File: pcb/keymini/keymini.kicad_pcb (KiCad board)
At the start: 2 copper layers, 205.4 x 88.6 mm, 86 parts, among them J1 USB_C_Receptacle_USB2.0_16P, SW1A1 SW_Push, SW1B1 SW_Push, SW1C1 SW_Push, SW1D1 SW_Push, SW1E1 SW_Push, SW1F1 SW_Push, SW1G1 SW_Push, SW1H1 SW_Push, SW1I1 SW_Push, SW1J1 SW_Push, SW2A1 SW_Push, SW2B1 SW_Push, SW2C1 SW_Push, SW2D1 SW_Push, SW2E1 SW_Push, SW2F1 SW_Push, SW2G1 SW_Push, SW2H1 SW_Push, SW2I1 SW_Push, SW2J1 SW_Push, SW3A1 SW_Push, SW3B1 SW_Push, SW3C1 SW_Push, SW3D1 SW_Push, SW3E1 SW_Push, SW3F1 SW_Push, SW3G1 SW_Push, SW3H1 SW_Push, SW3I1 SW_Push, SW3J1 SW_Push, SW4C1 SW_Push, SW4D1 SW_Push, SW4E1 SW_Push, SW4F1 SW_Push, SW4G1 SW_Push, SW4H1 SW_Push, U1 STM32F072CBT6, U2 XC6206P332MR

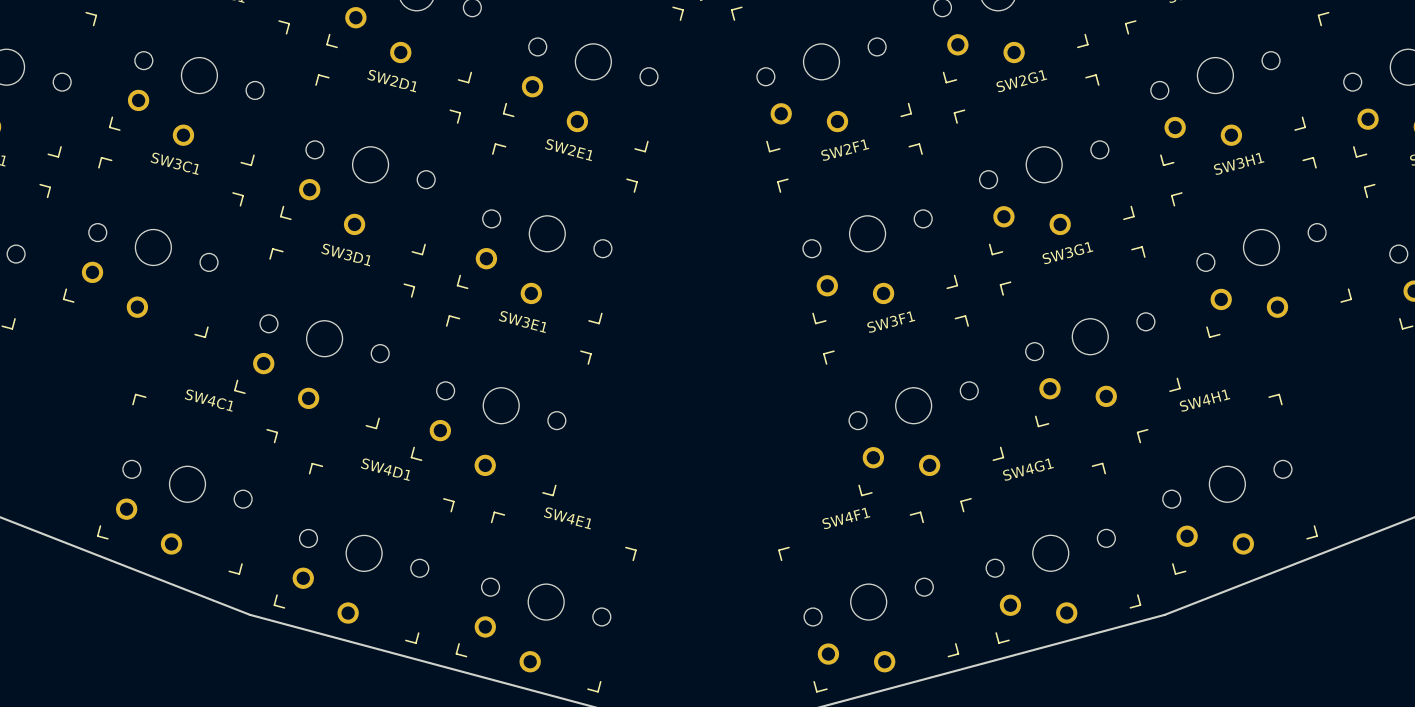
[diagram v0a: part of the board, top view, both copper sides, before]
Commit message: key placement corrections
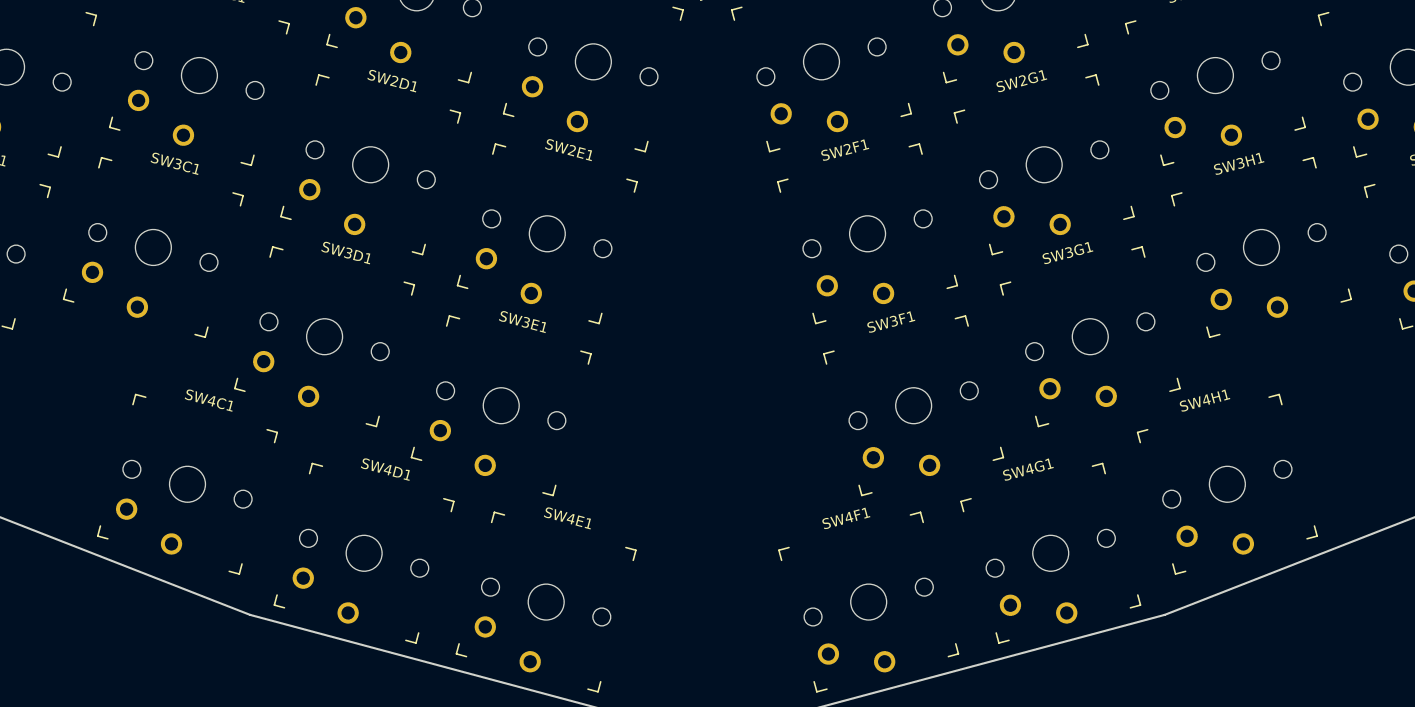
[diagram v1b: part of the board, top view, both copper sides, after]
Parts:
- moved SW3D1 0.19 mm to (113.4, 72.1)
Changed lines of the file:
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@@
 	(footprint "switch:SW_PG1350"
 		(layer "F.Cu")
-		(at 97.087 63.61 -15)
+		(at 97.086 63.609 -15)
 		(descr "Kailh \"Choc\" PG1350 keyswitch")
 		(tags "kailh,choc")
@@
 	(footprint "switch:SW_PG1350"
 		(layer "F.Cu")
-		(at 117.214 92.824 -15)
+		(at 117.214 92.814 -15)
 		(descr "Kailh \"Choc\" PG1350 keyswitch")
 		(tags "kailh,choc")
@@
 	(footprint "switch:SW_PG1350"
 		(layer "F.Cu")
-		(at 113.438 72.32 -15)
+		(at 113.438 72.132 -15)
 		(descr "Kailh \"Choc\" PG1350 keyswitch")
 		(tags "kailh,choc")
@@
 	(footprint "switch:SW_PG1350"
 		(layer "F.Cu")
-		(at 117.828 55.711 -15)
+		(at 117.838 55.711 -15)
 		(descr "Kailh \"Choc\" PG1350 keyswitch")
 		(tags "kailh,choc")
@@
 	(footprint "switch:SW_PG1350"
 		(layer "F.Cu")
-		(at 202.914 63.61 15)
+		(at 202.914 63.609 15)
 		(descr "Kailh \"Choc\" PG1350 keyswitch")
 		(tags "kailh,choc")

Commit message: A bit of diode placement
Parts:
- moved D1I1 112.9 mm to (211.3, 25.4), turned to 15 degrees
- moved D1H1 112.7 mm to (192.9, 26.2), turned to 15 degrees
- moved D1B1 112.6 mm to (88.7, 25.4), turned to -15 degrees
- moved D1C1 112.0 mm to (107.1, 26.2), turned to -15 degrees
- moved D1J1 105.6 mm to (231.8, 32.4), turned to 15 degrees
- moved D1A1 105.3 mm to (68.2, 32.4), turned to -15 degrees
- moved D1D1 103.6 mm to (123.5, 34.8), turned to -15 degrees
- moved D1G1 101.9 mm to (176.5, 34.8), turned to 15 degrees
- moved D1E1 96.7 mm to (140.3, 41.3), turned to -15 degrees
- moved D1F1 95.6 mm to (159.7, 41.3), turned to 15 degrees
- moved SW1J1 1.00 mm to (233.0, 36.9)

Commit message: more diode placement
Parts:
- moved D2I1 112.6 mm to (215.7, 41.9), turned to 15 degrees
- moved D2H1 112.4 mm to (197.3, 42.6), turned to 15 degrees
- moved D2B1 112.3 mm to (84.3, 41.9), turned to -15 degrees
- moved D2C1 111.3 mm to (102.7, 42.6), turned to -15 degrees
- moved D2J1 105.2 mm to (236.2, 48.8), turned to 15 degrees
- moved D2A1 104.9 mm to (63.8, 48.8), turned to -15 degrees
- moved D2G1 103.9 mm to (180.9, 51.2), turned to 15 degrees
- moved D2D1 103.2 mm to (119.1, 51.2), turned to -15 degrees
- moved D2F1 97.4 mm to (164.1, 57.8), turned to 15 degrees
- moved D2E1 96.3 mm to (135.9, 57.8), turned to -15 degrees

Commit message: diode placement: all done
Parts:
- moved D3I1 113.4 mm to (220.1, 58.3), turned to 15 degrees
- moved D3H1 113.2 mm to (201.7, 59.1), turned to 15 degrees
- moved D3B1 112.2 mm to (79.9, 58.3), turned to -15 degrees
- moved D3C1 110.9 mm to (98.3, 59.1), turned to -15 degrees
- moved D4H1 110.4 mm to (198.4, 81.7), turned to 15 degrees
- moved D4C1 108.7 mm to (101.6, 81.7), turned to -15 degrees
- moved D3J1 106.4 mm to (240.6, 65.2), turned to 15 degrees
- moved D3A1 104.8 mm to (59.4, 65.2), turned to -15 degrees
- moved D3G1 104.6 mm to (185.3, 67.6), turned to 15 degrees
- moved D4G1 104.4 mm to (181.6, 88.3), turned to 15 degrees
- moved D3D1 102.4 mm to (114.7, 67.6), turned to -15 degrees
- moved D4D1 102.1 mm to (118.4, 88.3), turned to -15 degrees
- moved D4F1 99.5 mm to (164.2, 92.9), turned to 15 degrees
- moved D3F1 98.8 mm to (168.5, 74.2), turned to 15 degrees
- moved D4E1 97.6 mm to (135.8, 92.9), turned to -15 degrees
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
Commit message: composant placement
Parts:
- removed SWB2: SW_Push, Button_Switch_SMD:SW_SPST_CK_RS282G05A3
- BOOT: renamed from SWB1; moved to B.Cu
- moved BOOT 94.0 mm to (150.1, 88.0), turned to 180 degrees
- moved R2 91.1 mm to (149.0, 55.9), turned to 90 degrees
- moved R1 89.9 mm to (151.0, 55.9), turned to -90 degrees
- moved R3 86.0 mm to (150.0, 90.0)
- moved C5 69.1 mm to (144.0, 87.0), turned to 180 degrees
- moved C4 69.0 mm to (156.0, 87.0), turned to 180 degrees
- moved C6 69.0 mm to (144.0, 75.0)
- moved U1 69.0 mm to (150.0, 81.0)
- moved C3 68.9 mm to (156.0, 75.0), turned to 0 degrees
- moved C2 63.0 mm to (150.0, 70.0)
- moved U2 62.0 mm to (150.0, 66.0)
- moved C1 61.0 mm to (150.0, 62.0), turned to 0 degrees
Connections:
- C1 pad 1: +5V -> GND
- C1 pad 2: GND -> +5V
- C4 pad 1: GND -> +3.3V
- C4 pad 2: +3.3V -> GND
- R2 pad 1: Net-(J1-CC2) -> GND
- R2 pad 2: GND -> Net-(J1-CC2)

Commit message: rename switches and diodes
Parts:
- renumbered D1A1 to D1A, D1B1 to D1B, D1C1 to D1C, D1D1 to D1D, D1E1 to D1E, D1F1 to D1F, D1G1 to D1G, D1H1 to D1H, D1I1 to D1I, D1J1 to D1J, D2A1 to D2A, D2B1 to D2B, D2C1 to D2C, D2D1 to D2D, D2E1 to D2E, D2F1 to D2F, D2G1 to D2G, D2H1 to D2H, D2I1 to D2I, D2J1 to D2J, D3A1 to D3A, D3B1 to D3B, D3C1 to D3C, D3D1 to D3D, D3E1 to D3E, D3F1 to D3F, D3G1 to D3G, D3H1 to D3H, D3I1 to D3I, D3J1 to D3J, D4C1 to D4C, D4D1 to D4D, D4E1 to D4E, D4F1 to D4F, D4G1 to D4G, D4H1 to D4H, SW1A1 to SW1A, SW1B1 to SW1B, SW1C1 to SW1C, SW1D1 to SW1D, SW1E1 to SW1E, SW1F1 to SW1F, SW1G1 to SW1G, SW1H1 to SW1H, SW1I1 to SW1I, SW1J1 to SW1J, SW2A1 to SW2A, SW2B1 to SW2B, SW2C1 to SW2C, SW2D1 to SW2D, SW2E1 to SW2E, SW2F1 to SW2F, SW2G1 to SW2G, SW2H1 to SW2H, SW2I1 to SW2I, SW2J1 to SW2J, SW3A1 to SW3A, SW3B1 to SW3B, SW3C1 to SW3C, SW3D1 to SW3D, SW3E1 to SW3E, SW3F1 to SW3F, SW3G1 to SW3G, SW3H1 to SW3H, SW3I1 to SW3I, SW3J1 to SW3J, SW4C1 to SW4C, SW4D1 to SW4D, SW4E1 to SW4E, SW4F1 to SW4F, SW4G1 to SW4G, SW4H1 to SW4H

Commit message: a lot of traces
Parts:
- moved R1 1.00 mm to (152.0, 55.9)
- moved R2 1.00 mm to (148.0, 55.9)
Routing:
- net ROW1: track 0.00 -> 279.7 mm
- net ROW2: track 0.00 -> 251.3 mm
- net ROW3: track 0.00 -> 225.7 mm
- net ROW4: track 0.00 -> 106.9 mm
- net +3.3V: track 0.00 -> 82.9 mm, vias 0 -> 1
- net COLC: track 0.00 -> 60.5 mm
- net COLH: track 0.00 -> 60.5 mm
- net GND: track 0.00 -> 60.0 mm
- net COLD: track 0.00 -> 58.7 mm
- net COLG: track 0.00 -> 58.7 mm
- net COLE: track 0.00 -> 57.0 mm
- net COLF: track 0.00 -> 57.0 mm
- net D+: track 0.00 -> 43.3 mm
- net D-: track 0.00 -> 43.1 mm
- net COLJ: track 0.00 -> 36.5 mm
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
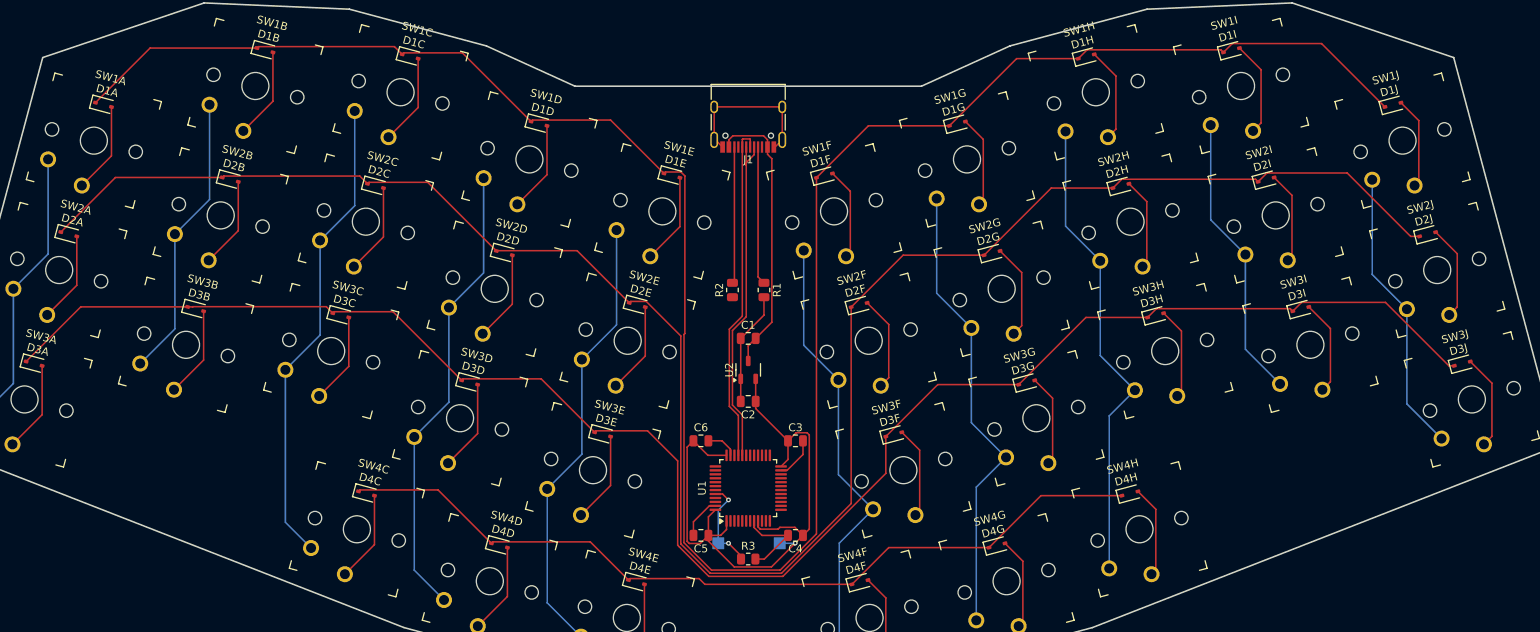
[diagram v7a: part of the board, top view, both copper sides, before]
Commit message: rows and cols connected
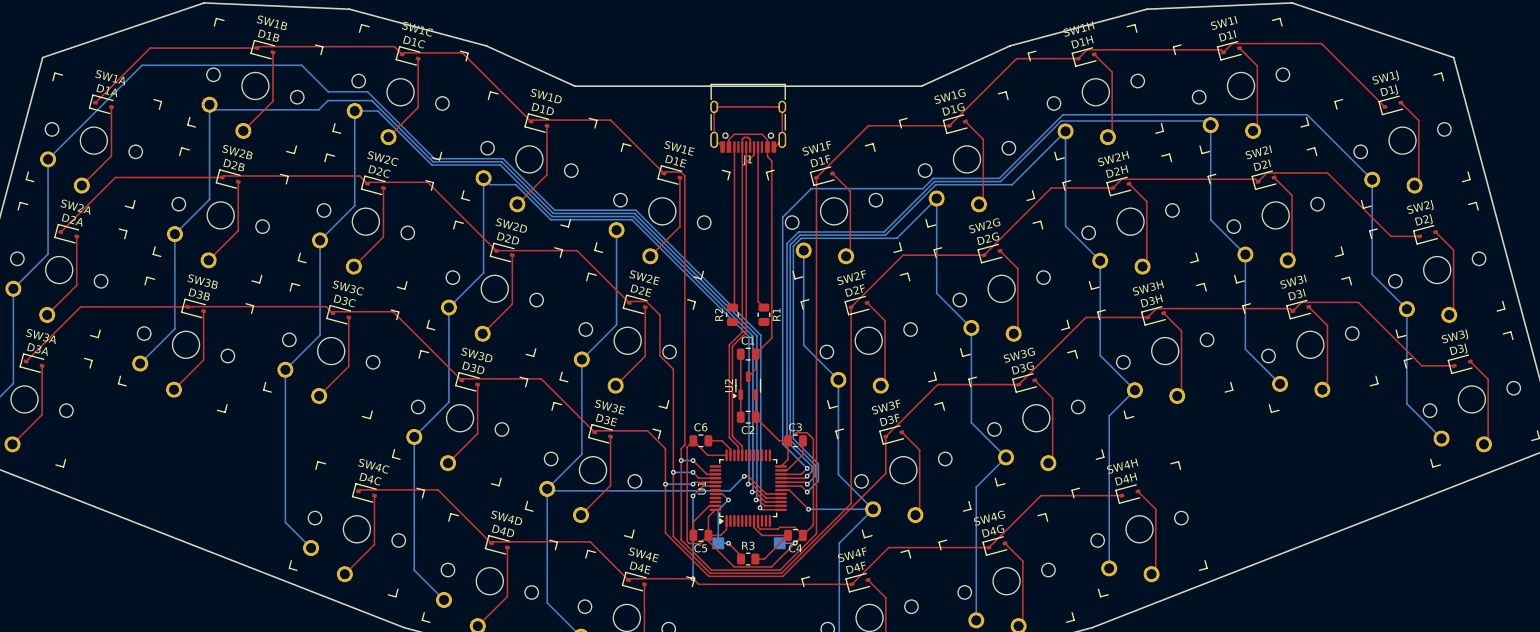
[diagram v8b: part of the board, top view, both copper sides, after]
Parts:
- moved R1 3.14 mm to (152.0, 59.0)
- moved R2 3.14 mm to (148.0, 59.0)
- moved C1 2.00 mm to (150.0, 64.0)
- moved C2 2.00 mm to (150.0, 72.0)
- moved U2 2.00 mm to (150.0, 68.0)
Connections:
- U1 pad 13: unconnected-(U1-PA3-Pad13) -> COLA
- U1 pad 14: unconnected-(U1-PA4-Pad14) -> COLB
- U1 pad 15: unconnected-(U1-PA5-Pad15) -> COLC
- U1 pad 16: unconnected-(U1-PA6-Pad16) -> COLD
- U1 pad 17: unconnected-(U1-PA7-Pad17) -> COLE
- U1 pad 18: unconnected-(U1-PB0-Pad18) -> COLF
- U1 pad 19: unconnected-(U1-PB1-Pad19) -> COLG
- U1 pad 20: unconnected-(U1-PB2-Pad20) -> COLH
- U1 pad 21: unconnected-(U1-PB10-Pad21) -> COLI
- U1 pad 22: unconnected-(U1-PB11-Pad22) -> COLJ
- U1 pad 39: unconnected-(U1-PB3-Pad39) -> ROW1
- U1 pad 40: unconnected-(U1-PB4-Pad40) -> ROW2
- U1 pad 41: unconnected-(U1-PB5-Pad41) -> ROW3
- U1 pad 42: unconnected-(U1-PB6-Pad42) -> ROW4
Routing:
- net COLA: track 36.5 -> 170.8 mm, vias 0 -> 1
- net COLJ: track 36.5 -> 156.9 mm, vias 0 -> 1
- net COLB: track 36.5 -> 143.4 mm, vias 0 -> 1
- net COLI: track 36.5 -> 131.4 mm, vias 0 -> 1
- net COLC: track 60.5 -> 146.8 mm, vias 0 -> 1
- net COLH: track 60.5 -> 136.9 mm, vias 0 -> 1
- net COLD: track 58.7 -> 124.4 mm, vias 0 -> 1
- net COLG: track 58.7 -> 116.2 mm, vias 0 -> 1
- net COLE: track 57.0 -> 88.5 mm, vias 0 -> 1
- net ROW4: track 106.9 -> 120.7 mm, vias 0 -> 2
- net COLF: track 57.0 -> 69.7 mm, vias 0 -> 1
- net ROW3: track 225.7 -> 233.7 mm, vias 0 -> 2
- net GND: track 60.0 -> 53.6 mm
- net ROW2: track 251.3 -> 256.9 mm, vias 0 -> 2
- net ROW1: track 279.7 -> 285.0 mm, vias 0 -> 2
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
